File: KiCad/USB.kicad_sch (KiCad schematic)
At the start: 2 parts, among them U2 HT42B534-2

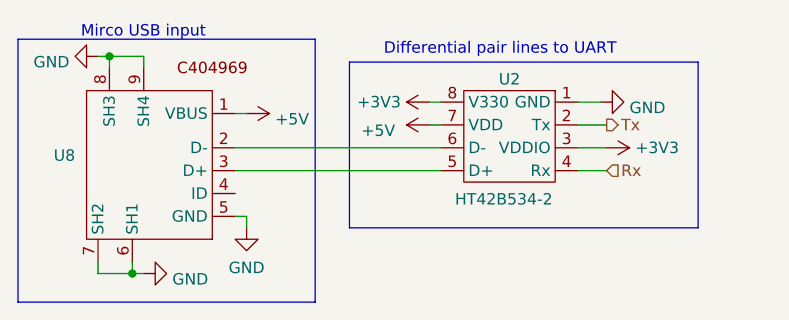
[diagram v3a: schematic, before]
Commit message: Added testpoint and changed headers to 0Ωs
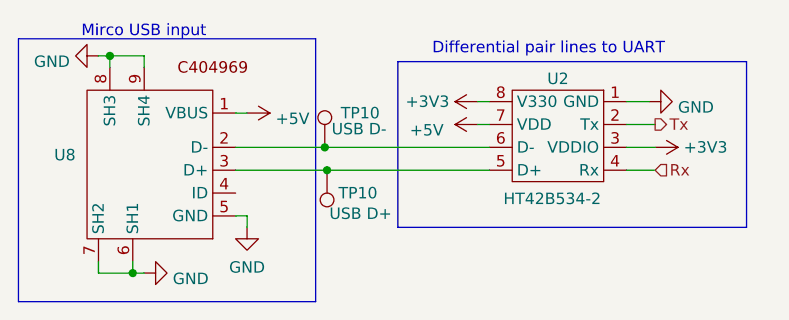
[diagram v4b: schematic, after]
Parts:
- added TP10: USB D+, symbol Connector:TestPoint
- added TP10: USB D-, symbol Connector:TestPoint
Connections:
- net at U2.5 (D+), U8.3 (D+): now also TP10.1
- net at U2.6 (D-), U8.2 (D-): now also TP10.1
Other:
- moved on the sheet: U2

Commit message: changed a bunch of net labels, changed some uc schem stuff
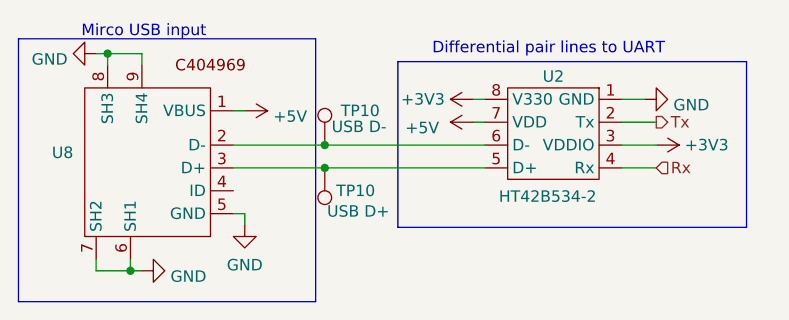
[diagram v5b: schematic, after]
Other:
- moved on the sheet: U2

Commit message: updated net labelling scheme on schematic, changed some port connections on microcontroller
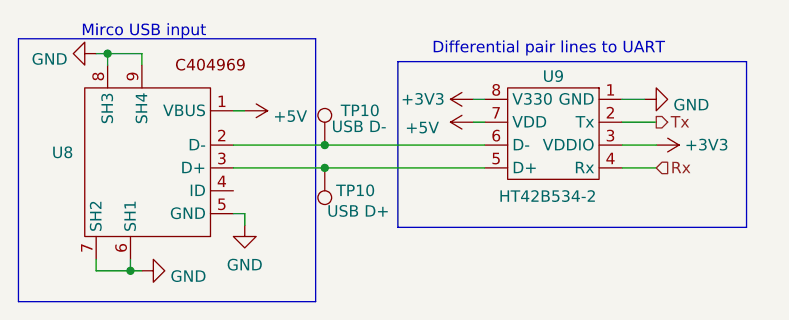
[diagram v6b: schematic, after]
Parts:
- renumbered U2 to U9
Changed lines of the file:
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@@
   (symbol (lib_id "power:GND") (at 246.38 138.43 90) (unit 1)
     (in_bom yes) (on_board yes) (dnp no) (fields_autoplaced)
-    (property "Reference" "#PWR0107" (at 252.73 138.43 0)
+    (property "Reference" "#PWR054" (at 252.73 138.43 0)
       (effects (font (size 1.27 1.27)) hide)
     )
@@
       (project "EEE3088F_CKR"
         (path "/31e5d740-f3fb-4029-be8d-dfdc4f653d72/4be356fb-1e37-446a-bf93-f98ec62d54dd"
-          (reference "#PWR0107") (unit 1)
+          (reference "#PWR054") (unit 1)
         )
       )
@@
         )
         (path "/31e5d740-f3fb-4029-be8d-dfdc4f653d72/4be356fb-1e37-446a-bf93-f98ec62d54dd"
-          (reference "TP21") (unit 1)
+          (reference "TP28") (unit 1)
         )
       )
@@
         )
         (path "/31e5d740-f3fb-4029-be8d-dfdc4f653d72/4be356fb-1e37-446a-bf93-f98ec62d54dd"
-          (reference "TP22") (unit 1)
+          (reference "TP27") (unit 1)
         )
       )
@@
   (symbol (lib_id "power:+5V") (at 201.93 139.7 270) (unit 1)
     (in_bom yes) (on_board yes) (dnp no) (fields_autoplaced)
-    (property "Reference" "#PWR061" (at 198.12 139.7 0)
+    (property "Reference" "#PWR050" (at 198.12 139.7 0)
       (effects (font (size 1.27 1.27)) hide)
     )
@@
       (project "EEE3088F_CKR"
         (path "/31e5d740-f3fb-4029-be8d-dfdc4f653d72/4be356fb-1e37-446a-bf93-f98ec62d54dd"
-          (reference "#PWR061") (unit 1)
+          (reference "#PWR050") (unit 1)
         )
       )
@@
   (symbol (lib_id "power:+3V3") (at 247.65 143.51 270) (unit 1)
     (in_bom yes) (on_board yes) (dnp no)
-    (property "Reference" "#PWR065" (at 243.84 143.51 0)
+    (property "Reference" "#PWR055" (at 243.84 143.51 0)
       (effects (font (size 1.27 1.27)) hide)
     )
@@
       (project "EEE3088F_CKR"
         (path "/31e5d740-f3fb-4029-be8d-dfdc4f653d72/4be356fb-1e37-446a-bf93-f98ec62d54dd"
-          (reference "#PWR065") (unit 1)
+          (reference "#PWR055") (unit 1)
         )
       )
@@
   (symbol (lib_id "EEE3088F_CKR:HT42B534-2") (at 236.22 142.24 0) (mirror y) (unit 1)
     (in_bom yes) (on_board yes) (dnp no)
-    (property "Reference" "U2" (at 236.22 135.89 0)
+    (property "Reference" "U9" (at 236.22 135.89 0)
       (effects (font (size 1.27 1.27)))
     )
@@
       (project "EEE3088F_CKR"
         (path "/31e5d740-f3fb-4029-be8d-dfdc4f653d72/4be356fb-1e37-446a-bf93-f98ec62d54dd"
-          (reference "U2") (unit 1)
+          (reference "U9") (unit 1)
         )
       )
@@
         )
         (path "/31e5d740-f3fb-4029-be8d-dfdc4f653d72/4be356fb-1e37-446a-bf93-f98ec62d54dd"
-          (reference "U5") (unit 1)
+          (reference "U8") (unit 1)
         )
       )
@@
   (symbol (lib_id "power:GND") (at 190.5 157.48 90) (unit 1)
     (in_bom yes) (on_board yes) (dnp no) (fields_autoplaced)
-    (property "Reference" "#PWR0108" (at 196.85 157.48 0)
+    (property "Reference" "#PWR049" (at 196.85 157.48 0)
       (effects (font (size 1.27 1.27)) hide)
     )
@@
       (project "EEE3088F_CKR"
         (path "/31e5d740-f3fb-4029-be8d-dfdc4f653d72/4be356fb-1e37-446a-bf93-f98ec62d54dd"
-          (reference "#PWR0108") (unit 1)
+          (reference "#PWR049") (unit 1)
         )
       )
@@
   (symbol (lib_id "power:GND") (at 201.93 152.4 0) (unit 1)
     (in_bom yes) (on_board yes) (dnp no) (fields_autoplaced)
-    (property "Reference" "#PWR0110" (at 201.93 158.75 0)
+    (property "Reference" "#PWR051" (at 201.93 158.75 0)
       (effects (font (size 1.27 1.27)) hide)
     )
@@
       (project "EEE3088F_CKR"
         (path "/31e5d740-f3fb-4029-be8d-dfdc4f653d72/4be356fb-1e37-446a-bf93-f98ec62d54dd"
-          (reference "#PWR0110") (unit 1)
+          (reference "#PWR051") (unit 1)
         )
       )
@@
   (symbol (lib_id "power:GND") (at 185.42 133.35 270) (unit 1)
     (in_bom yes) (on_board yes) (dnp no) (fields_autoplaced)
-    (property "Reference" "#PWR0109" (at 179.07 133.35 0)
+    (property "Reference" "#PWR048" (at 179.07 133.35 0)
       (effects (font (size 1.27 1.27)) hide)
     )
@@
       (project "EEE3088F_CKR"
         (path "/31e5d740-f3fb-4029-be8d-dfdc4f653d72/4be356fb-1e37-446a-bf93-f98ec62d54dd"
-          (reference "#PWR0109") (unit 1)
+          (reference "#PWR048") (unit 1)
         )
       )
@@
   (symbol (lib_id "power:+5V") (at 227.33 140.97 90) (unit 1)
     (in_bom yes) (on_board yes) (dnp no) (fields_autoplaced)
-    (property "Reference" "#PWR060" (at 231.14 140.97 0)
+    (property "Reference" "#PWR053" (at 231.14 140.97 0)
       (effects (font (size 1.27 1.27)) hide)
     )
@@
       (project "EEE3088F_CKR"
         (path "/31e5d740-f3fb-4029-be8d-dfdc4f653d72/4be356fb-1e37-446a-bf93-f98ec62d54dd"
-          (reference "#PWR060") (unit 1)
+          (reference "#PWR053") (unit 1)
         )
       )
@@
   (symbol (lib_id "power:+3V3") (at 227.33 138.43 90) (unit 1)
     (in_bom yes) (on_board yes) (dnp no)
-    (property "Reference" "#PWR059" (at 231.14 138.43 0)
+    (property "Reference" "#PWR052" (at 231.14 138.43 0)
       (effects (font (size 1.27 1.27)) hide)
     )
@@
       (project "EEE3088F_CKR"
         (path "/31e5d740-f3fb-4029-be8d-dfdc4f653d72/4be356fb-1e37-446a-bf93-f98ec62d54dd"
-          (reference "#PWR059") (unit 1)
-        )
-      )
+          (reference "#PWR052") (unit 1)
+        )
+      )

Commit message: ran ERCs and fixed the errors
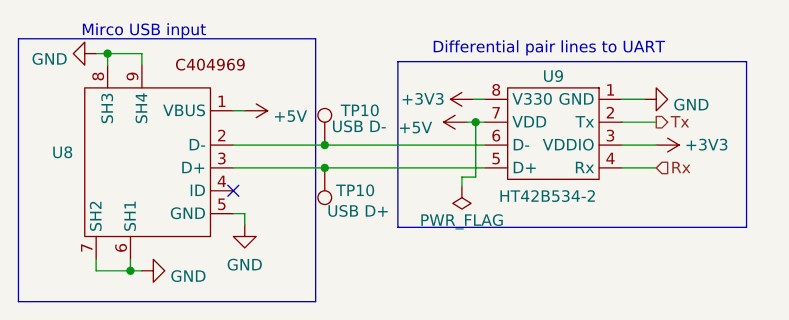
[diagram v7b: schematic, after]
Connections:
- no-connect marks 0 -> 1
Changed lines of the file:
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@@
   (junction (at 189.23 157.48) (diameter 0) (color 0 0 0 0)
   )
+  (junction (at 227.584 140.97) (diameter 0) (color 0 0 0 0)
+  )
+  (no_connect (at 200.66 148.59))
   (wire (pts (xy 190.5 133.35) (xy 190.5 134.62))
     (stroke (width 0) (type default))
@@
     (stroke (width 0) (type default))
   )
+  (wire (pts (xy 227.584 147.066) (xy 227.584 140.97))
+    (stroke (width 0) (type default))
+  )
   (wire (pts (xy 185.42 157.48) (xy 189.23 157.48))
     (stroke (width 0) (type default))
   )
+  (wire (pts (xy 226.06 148.082) (xy 226.06 147.066))
+    (stroke (width 0) (type default))
+  )
   (wire (pts (xy 227.33 138.43) (xy 228.6 138.43))
     (stroke (width 0) (type default))
@@
     (stroke (width 0) (type default))
   )
+  (wire (pts (xy 227.584 140.97) (xy 228.6 140.97))
+    (stroke (width 0) (type default))
+  )
   (wire (pts (xy 243.84 143.51) (xy 247.65 143.51))
     (stroke (width 0) (type default))
@@
     (stroke (width 0) (type default))
   )
+  (wire (pts (xy 226.06 147.066) (xy 227.584 147.066))
+    (stroke (width 0) (type default))
+  )
   (wire (pts (xy 185.42 133.35) (xy 186.69 133.35))
     (stroke (width 0) (type default))
   )
-  (wire (pts (xy 227.33 140.97) (xy 228.6 140.97))
+  (wire (pts (xy 226.568 140.97) (xy 227.584 140.97))
     (stroke (width 0) (type default))
   )
@@
         (path "/31e5d740-f3fb-4029-be8d-dfdc4f653d72/4be356fb-1e37-446a-bf93-f98ec62d54dd"
           (reference "#PWR054") (unit 1)
+        )
+      )
+    )
+  )
+  (symbol (lib_id "power:PWR_FLAG") (at 226.06 148.082 180) (unit 1)
+    (in_bom yes) (on_board yes) (dnp no)
+    (property "Reference" "#FLG07" (at 226.06 149.987 0)
+      (effects (font (size 1.27 1.27)) hide)
+    )
+    (property "Value" "PWR_FLAG" (at 226.06 151.892 0)
+      (effects (font (size 1.27 1.27)))
+    )
+    (property "Footprint" "" (at 226.06 148.082 0)
+      (effects (font (size 1.27 1.27)) hide)
+    )
+    (property "Datasheet" "~" (at 226.06 148.082 0)
+      (effects (font (size 1.27 1.27)) hide)
+    )
+    (pin "1")
+    (instances
+      (project "EEE3088F_CKR"
+        (path "/31e5d740-f3fb-4029-be8d-dfdc4f653d72/4be356fb-1e37-446a-bf93-f98ec62d54dd"
+          (reference "#FLG07") (unit 1)
         )
       )
@@
     )
   )
-  (symbol (lib_id "power:+5V") (at 227.33 140.97 90) (unit 1)
-    (in_bom yes) (on_board yes) (dnp no) (fields_autoplaced)
-    (property "Reference" "#PWR053" (at 231.14 140.97 0)
-      (effects (font (size 1.27 1.27)) hide)
-    )
-    (property "Value" "+5V" (at 223.52 141.605 90)
-      (effects (font (size 1.27 1.27)) (justify left))
-    )
-    (property "Footprint" "" (at 227.33 140.97 0)
-      (effects (font (size 1.27 1.27)) hide)
-    )
-    (property "Datasheet" "" (at 227.33 140.97 0)
-      (effects (font (size 1.27 1.27)) hide)
-    )
+  (symbol (lib_id "power:+5V") (at 226.568 140.97 90) (unit 1)
+    (in_bom yes) (on_board yes) (dnp no) (fields_autoplaced)
+    (property "Reference" "#PWR053" (at 230.378 140.97 0)
+      (effects (font (size 1.27 1.27)) hide)
+    )
+    (property "Value" "+5V" (at 222.758 141.605 90)
+      (effects (font (size 1.27 1.27)) (justify left))
+    )
+    (property "Footprint" "" (at 226.568 140.97 0)
+      (effects (font (size 1.27 1.27)) hide)
+    )
+    (property "Datasheet" "" (at 226.568 140.97 0)
+      (effects (font (size 1.27 1.27)) hide)
+    )

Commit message: bom updated and test labes renamed
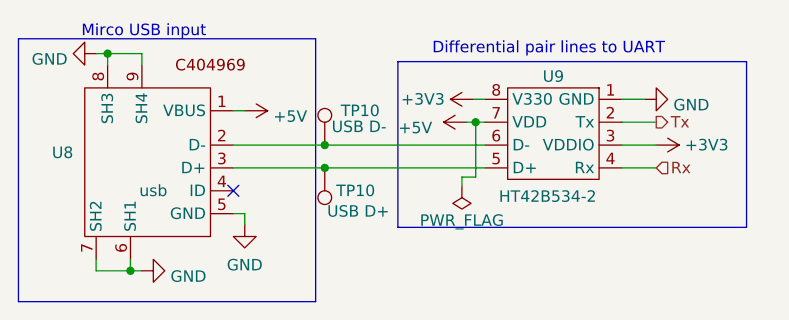
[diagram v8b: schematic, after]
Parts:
- TP10: Extended Part Cost (none) -> 0; cost per unit (none) -> 0
- U8: value ~ -> usb; Extended Part Cost (none) -> 3; JLC code (none) -> C404969; Part name (none) -> MicroXNJ; cost per unit (none) -> 0.0333
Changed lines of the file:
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@@
+      (effects (font (size 1.27 1.27)) hide)
+    )
+    (property "Extended Part Cost" "0" (at 210.82 146.05 0)
+      (effects (font (size 1.27 1.27)) hide)
+    )
+    (property "cost per unit" "0" (at 210.82 146.05 0)
       (effects (font (size 1.27 1.27)) hide)
     )
@@
     )
     (property "Datasheet" "~" (at 215.9 143.51 0)
+      (effects (font (size 1.27 1.27)) hide)
+    )
+    (property "Extended Part Cost" "0" (at 210.82 143.51 0)
+      (effects (font (size 1.27 1.27)) hide)
+    )
+    (property "cost per unit" "0" (at 210.82 143.51 0)
       (effects (font (size 1.27 1.27)) hide)
     )
@@
       (effects (font (size 1.27 1.27)) (justify left))
     )
-    (property "Value" "~" (at 191.77 148.59 0)
+    (property "Value" "usb" (at 191.77 148.59 0)
       (effects (font (size 1.27 1.27)))
     )
@@
       (effects (font (size 1.27 1.27)) hide)
     )
-    (property "Extended Part Cost" "" (at 191.77 148.59 0)
+    (property "Extended Part Cost" "3" (at 191.77 148.59 0)
       (effects (font (size 1.27 1.27)) hide)
     )
-    (property "JLC code" "" (at 191.77 148.59 0)
+    (property "JLC code" "C404969" (at 191.77 148.59 0)
       (effects (font (size 1.27 1.27)) hide)
     )
-    (property "Part name" "" (at 191.77 148.59 0)
+    (property "Part name" "MicroXNJ" (at 191.77 148.59 0)
       (effects (font (size 1.27 1.27)) hide)
     )
-    (property "cost per unit" "" (at 191.77 148.59 0)
+    (property "cost per unit" "0.0333" (at 191.77 148.59 0)
       (effects (font (size 1.27 1.27)) hide)
     )
